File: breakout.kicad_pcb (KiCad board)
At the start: 2 copper layers, 103 x 62 mm, 32 parts, among them CON1 SD_Card, CON2 USB-MICRO-AB, P2 CONN_01X40, P3 CONN_01X40, P4 CONN_01X40, P5 A-DF-09-A/KG-T4S, Q1 SIA461DJ-T1-GE3, SW1 SW_PUSH

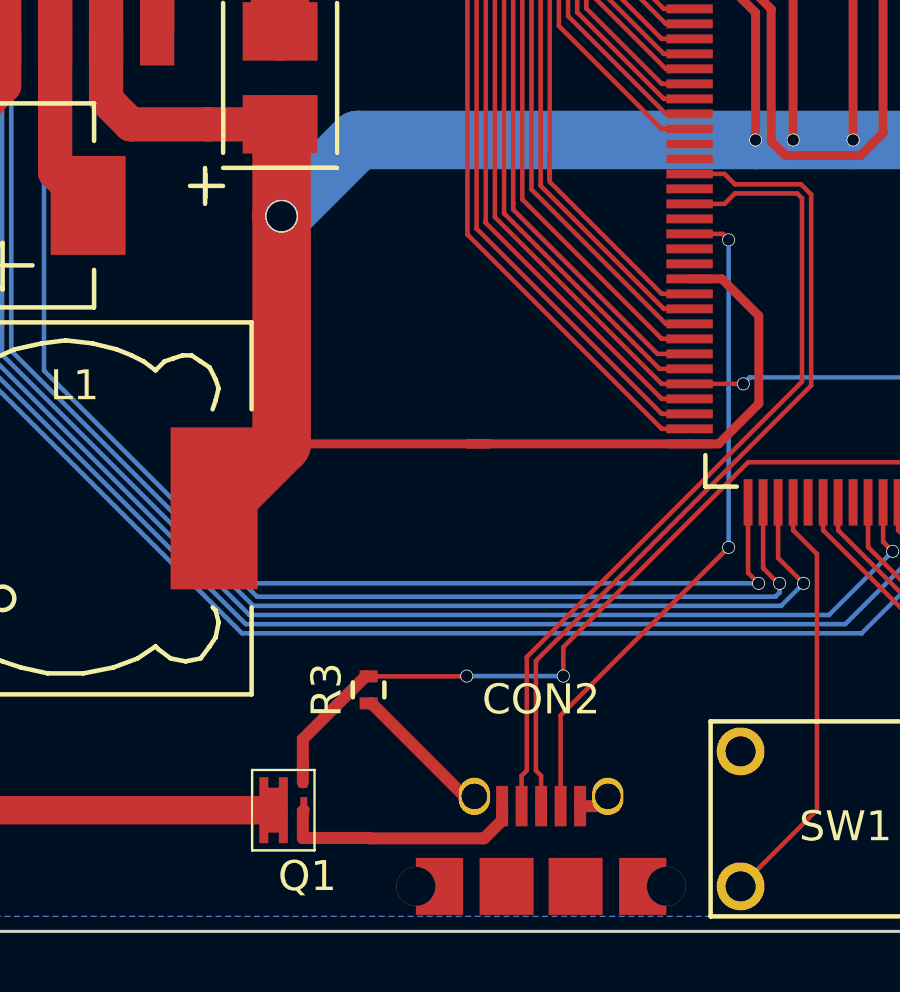
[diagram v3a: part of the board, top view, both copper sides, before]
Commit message: added USB FET to schematic and board
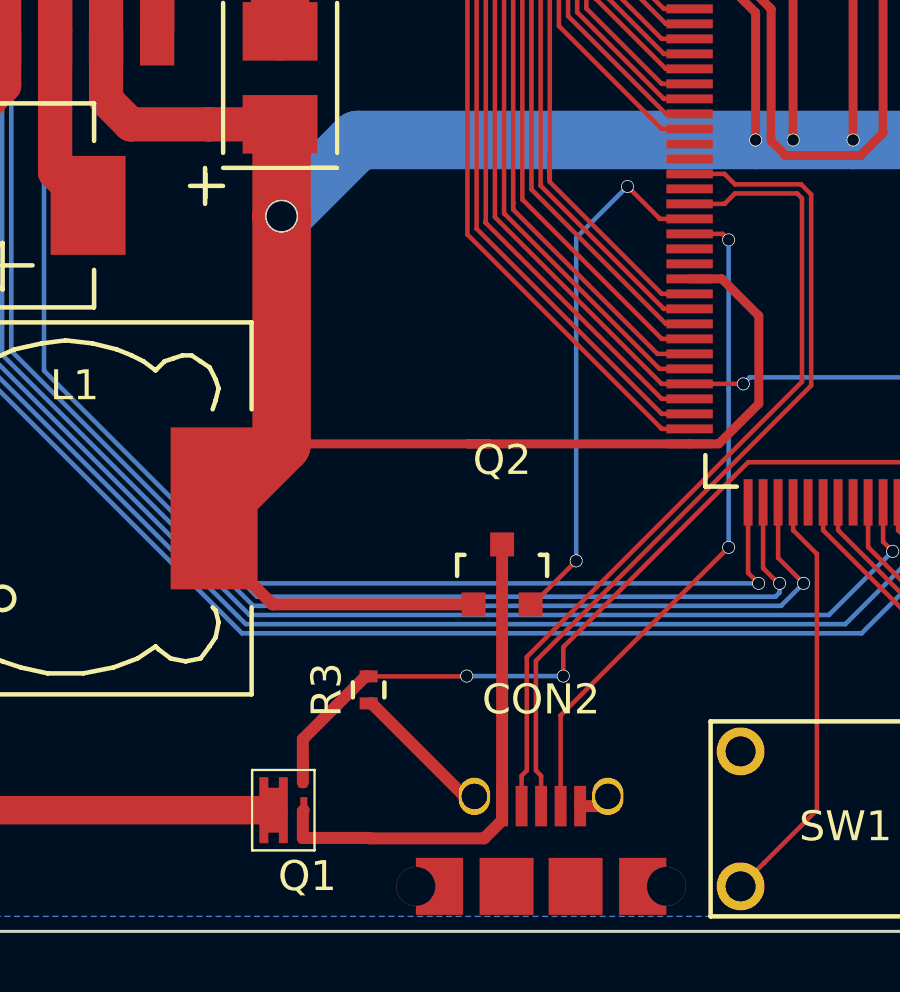
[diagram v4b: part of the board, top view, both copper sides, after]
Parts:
- added Q2: IRLML2402TRPBF, Housings_SOT-23_SOT-143_TSOT-6:SOT-23, F.Cu at (93.0, 163.1)
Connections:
- net Net-(CON2-Pad1) renamed /USB0_VBUS_PR
- CPU1 pad 21: (no net) -> /USB0_VBUS
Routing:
- net /USB0_VBUS: track 0.00 -> 17.8 mm, vias 0 -> 2
- net /3.3V: track 243.1 -> 253.8 mm
- net /USB0_VBUS_PR: track 8.31 -> 17.0 mm

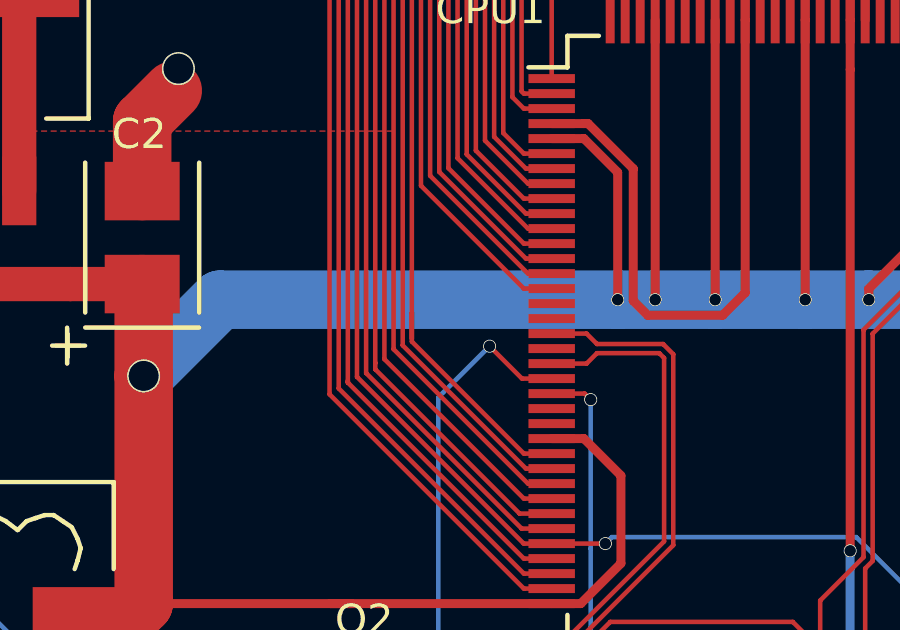
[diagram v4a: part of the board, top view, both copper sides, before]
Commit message: added USB0_RREF and 12K resistor
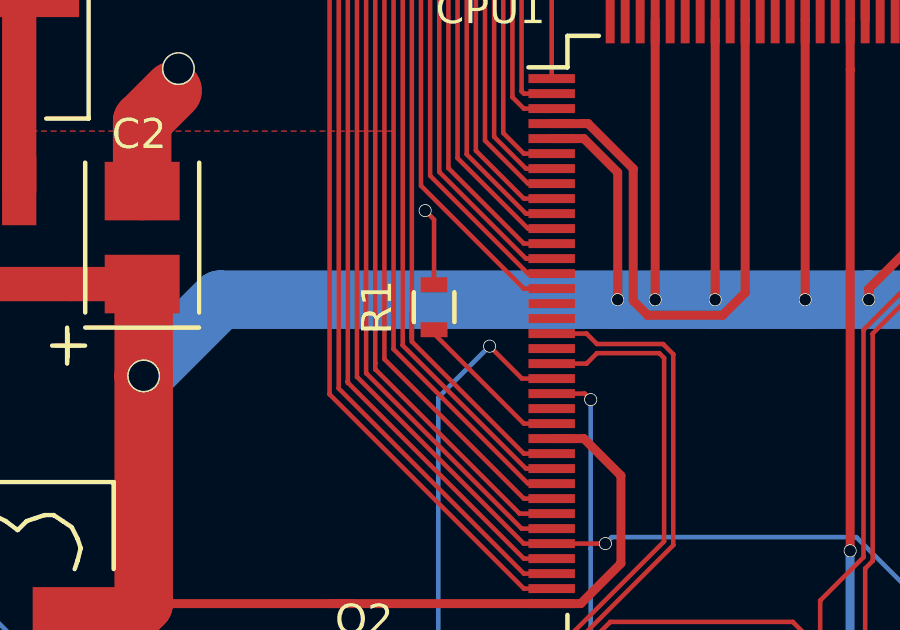
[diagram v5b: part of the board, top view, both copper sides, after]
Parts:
- added R1: 12K, Resistors_SMD:R_0603, F.Cu at (95.4, 148.9)
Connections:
- CPU1 pad 24: (no net) -> /USB0_RREF
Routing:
- net /USB0_RREF: track 0.00 -> 5.30 mm
- net GND: track 136.9 -> 139.5 mm, vias 8 -> 9

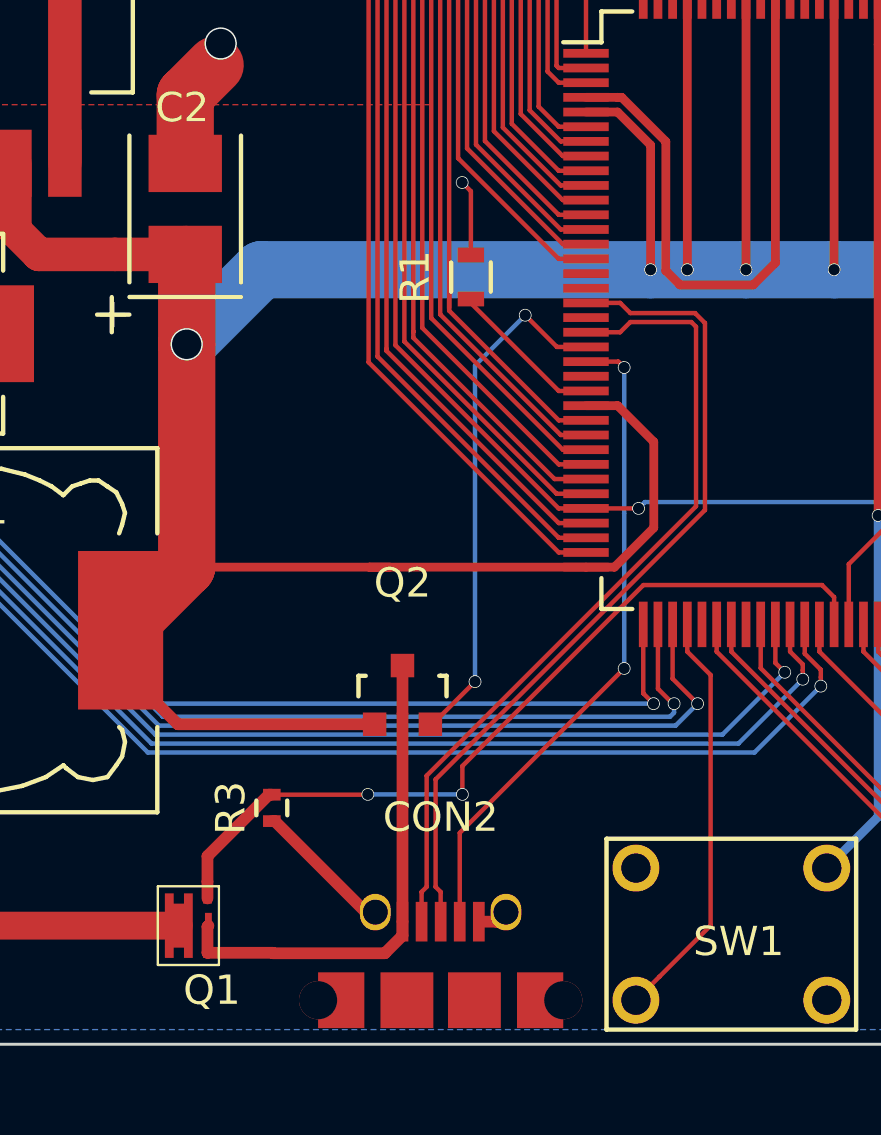
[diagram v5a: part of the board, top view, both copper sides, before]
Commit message: added the NC'd USB0 pins, and fixed some trace sizes
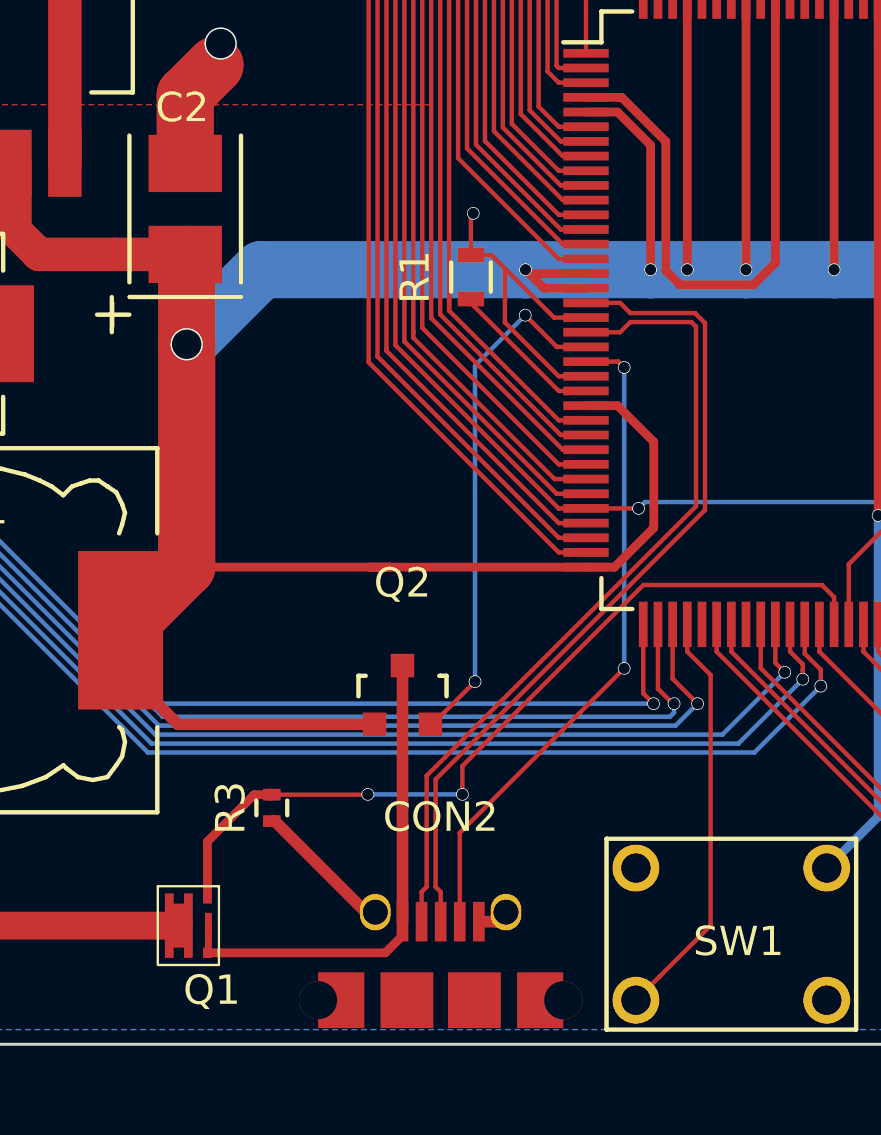
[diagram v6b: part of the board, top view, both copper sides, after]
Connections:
- CPU1 pad 16: (no net) -> /3.3V
- CPU1 pad 17: (no net) -> /3.3V
- CPU1 pad 19: (no net) -> GND
- CPU1 pad 23: (no net) -> GND
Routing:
- net GND: track 139.5 -> 148.6 mm
- net /3.3V: track 253.8 -> 258.3 mm, vias 10 -> 11
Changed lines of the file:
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@@
 (kicad_pcb (version 4) (host pcbnew "(after 2015-mar-04 BZR unknown)-product")
   (general
-    (links 234)
+    (links 238)
     (no_connects 19)
     (area 57.949999 112.949999 161.050001 175.050001)
     (thickness 1.6)
     (drawings 11)
-    (tracks 1106)
+    (tracks 1118)
     (zones 0)
     (modules 34)
@@
     (pad 15 smd rect (at -10.7 -1.75) (size 1.55 0.3) (layers F.Cu F.Paste F.Mask)
       (net 45 /P4_8))
-    (pad 16 smd rect (at -10.7 -1.25) (size 1.55 0.3) (layers F.Cu F.Paste F.Mask))
-    (pad 17 smd rect (at -10.7 -0.75) (size 1.55 0.3) (layers F.Cu F.Paste F.Mask))
+    (pad 16 smd rect (at -10.7 -1.25) (size 1.55 0.3) (layers F.Cu F.Paste F.Mask)
+      (net 4 /3.3V))
+    (pad 17 smd rect (at -10.7 -0.75) (size 1.55 0.3) (layers F.Cu F.Paste F.Mask)
+      (net 4 /3.3V))
     (pad 18 smd rect (at -10.7 -0.25) (size 1.55 0.3) (layers F.Cu F.Paste F.Mask)
       (net 29 /USB0_D+))
-    (pad 19 smd rect (at -10.7 0.25) (size 1.55 0.3) (layers F.Cu F.Paste F.Mask))
+    (pad 19 smd rect (at -10.7 0.25) (size 1.55 0.3) (layers F.Cu F.Paste F.Mask)
+      (net 1 GND))
     (pad 20 smd rect (at -10.7 0.75) (size 1.55 0.3) (layers F.Cu F.Paste F.Mask)
       (net 28 /USB0_D-))
@@
     (pad 22 smd rect (at -10.7 1.75) (size 1.55 0.3) (layers F.Cu F.Paste F.Mask)
       (net 30 /USB0_ID))
-    (pad 23 smd rect (at -10.7 2.25) (size 1.55 0.3) (layers F.Cu F.Paste F.Mask))
+    (pad 23 smd rect (at -10.7 2.25) (size 1.55 0.3) (layers F.Cu F.Paste F.Mask)
+      (net 1 GND))
     (pad 24 smd rect (at -10.7 2.75) (size 1.55 0.3) (layers F.Cu F.Paste F.Mask)
       (net 133 /USB0_RREF))
@@
   (gr_line (start 58 113) (end 161 113) (angle 90) (layer Edge.Cuts) (width 0.1))
   (segment (start 65.08 125.84114) (end 65.08 125) (width 0.1524) (layer F.Cu) (net 0))
-  (segment (start 95.38 148.12) (end 95.38 145.946811) (width 0.1524) (layer F.Cu) (net 1))
-  (segment (start 95.38 145.946811) (end 95.083189 145.65) (width 0.1524) (layer F.Cu) (net 1))
-  (via (at 95.083189 145.65) (size 0.4318) (drill 0.381) (layers F.Cu B.Cu) (net 1))
+  (segment (start 95.38 148.12) (end 95.38 146.78) (width 0.1524) (layer F.Cu) (net 1))
+  (segment (start 95.38 146.78) (end 95.46 146.7) (width 0.1524) (layer F.Cu) (net 1))
+  (via (at 95.46 146.7) (size 0.4318) (drill 0.381) (layers F.Cu B.Cu) (net 1))
+  (segment (start 98.212099 150.25) (end 96.537853 148.575754) (width 0.1524) (layer F.Cu) (net 1))
+  (segment (start 96.537853 148.575754) (end 96.082099 148.12) (width 0.1524) (layer F.Cu) (net 1))
+  (segment (start 99.3 152.25) (end 98.3726 152.25) (width 0.1524) (layer F.Cu) (net 1))
+  (segment (start 98.3726 152.25) (end 96.537853 150.415253) (width 0.1524) (layer F.Cu) (net 1))
+  (segment (start 96.537853 150.415253) (end 96.537853 148.575754) (width 0.1524) (layer F.Cu) (net 1))
+  (segment (start 99.3 150.25) (end 98.212099 150.25) (width 0.1524) (layer F.Cu) (net 1))
+  (segment (start 96.082099 148.12) (end 95.9824 148.12) (width 0.1524) (layer F.Cu) (net 1))
+  (segment (start 95.9824 148.12) (end 95.38 148.12) (width 0.1524) (layer F.Cu) (net 1))
   (segment (start 88.6 167.4) (end 88.7 167.4) (width 0.4) (layer F.Cu) (net 1))
   (segment (start 88.7 167.4) (end 91.8 170.5) (width 0.4) (layer F.Cu) (net 1))
@@
   (segment (start 102.75 139.3) (end 102.75 148.62) (width 0.3) (layer F.Cu) (net 4))
   (via (at 102.75 148.62) (size 0.4318) (drill 0.381) (layers F.Cu B.Cu) (net 4))
-  (segment (start 88.24 148.62) (end 101.500445 148.62) (width 1.95072) (layer B.Cu) (net 4))
   (segment (start 100.375 143.25) (end 101.500445 144.375445) (width 0.3) (layer F.Cu) (net 4))
   (segment (start 99.3 143.25) (end 100.375 143.25) (width 0.3) (layer F.Cu) (net 4))
@@
   (segment (start 85.40108 164.10076) (end 83.45 162.14968) (width 0.4) (layer F.Cu) (net 4))
   (segment (start 92.1 164.10076) (end 85.40108 164.10076) (width 0.4) (layer F.Cu) (net 4))
+  (via (at 97.239961 148.62) (size 0.4318) (drill 0.381) (layers F.Cu B.Cu) (net 4))
+  (segment (start 97.869961 149.25) (end 97.239961 148.62) (width 0.3) (layer F.Cu) (net 4))
+  (segment (start 99.3 149.25) (end 97.869961 149.25) (width 0.3) (layer F.Cu) (net 4))
+  (segment (start 97.239961 148.62) (end 101.500445 148.62) (width 1.95072) (layer B.Cu) (net 4))
+  (segment (start 88.24 148.62) (end 97.239961 148.62) (width 1.95072) (layer B.Cu) (net 4))
+  (segment (start 97.369961 148.75) (end 97.239961 148.62) (width 0.3) (layer F.Cu) (net 4))
+  (segment (start 99.3 148.75) (end 97.369961 148.75) (width 0.3) (layer F.Cu) (net 4))
   (segment (start 122.2 157.7) (end 120.75 157.7) (width 0.1524) (layer F.Cu) (net 5))
   (segment (start 120.75 157.7) (end 120.7 157.75) (width 0.1524) (layer F.Cu) (net 5))
@@
   (segment (start 60.8787 168.68188) (end 60.1287 169.43188) (width 0.3) (layer F.Cu) (net 16))
   (segment (start 60.1287 169.43188) (end 60.1287 170.179964) (width 0.3) (layer F.Cu) (net 16))
+  (segment (start 86.4075 170.035) (end 86.4075 168.0925) (width 0.3) (layer F.Cu) (net 17))
+  (segment (start 86.4075 168.0925) (end 88 166.5) (width 0.3) (layer F.Cu) (net 17))
+  (segment (start 88 166.5) (end 88.6 166.5) (width 0.3) (layer F.Cu) (net 17))
   (segment (start 88.6 166.5) (end 88.5 166.5) (width 0.4) (layer F.Cu) (net 17))
-  (segment (start 88.5 166.5) (end 86.4075 168.5925) (width 0.4) (layer F.Cu) (net 17))
-  (segment (start 86.4075 168.5925) (end 86.4075 169.46) (width 0.4) (layer F.Cu) (net 17))
-  (segment (start 86.4075 169.46) (end 86.4075 170.035) (width 0.4) (layer F.Cu) (net 17))
   (segment (start 95.09 166.49) (end 95.09 165.523518) (width 0.1524) (layer F.Cu) (net 17))
   (segment (start 95.09 165.523518) (end 101.253518 159.36) (width 0.1524) (layer F.Cu) (net 17))
@@
   (segment (start 72.7 121.1684) (end 72.7 120) (width 0.1524) (layer B.Cu) (net 130))
   (segment (start 73.84298 122.31138) (end 72.7 121.1684) (width 0.1524) (layer B.Cu) (net 130))
-  (segment (start 86.4075 171.885) (end 86.4075 170.9925) (width 0.4) (layer F.Cu) (net 131))
-  (segment (start 86.4075 170.9925) (end 86.44 170.96) (width 0.4) (layer F.Cu) (net 131))
-  (segment (start 88.64 171.9) (end 88.625 171.885) (width 0.4) (layer F.Cu) (net 131))
-  (segment (start 88.625 171.885) (end 86.4075 171.885) (width 0.4) (layer F.Cu) (net 131))
-  (segment (start 92.45 171.9) (end 93.05 171.3) (width 0.4) (layer F.Cu) (net 131))
-  (segment (start 88.64 171.9) (end 92.45 171.9) (width 0.4) (layer F.Cu) (net 131))
-  (segment (start 93.05 171.3) (end 93.05 170.825) (width 0.4) (layer F.Cu) (net 131))
+  (segment (start 86.4075 171.885) (end 92.465 171.885) (width 0.3) (layer F.Cu) (net 131))
+  (segment (start 92.465 171.885) (end 93.05 171.3) (width 0.3) (layer F.Cu) (net 131))
+  (segment (start 93.05 171.3) (end 93.05 170.825) (width 0.3) (layer F.Cu) (net 131))
+  (segment (start 86.44 170.96) (end 86.44 171.8525) (width 0.235) (layer F.Cu) (net 131))
+  (segment (start 86.44 171.8525) (end 86.4075 171.885) (width 0.235) (layer F.Cu) (net 131))
   (segment (start 93.05 163.753498) (end 93.05 162.10178) (width 0.4) (layer F.Cu) (net 131))
   (segment (start 93.05 170.825) (end 93.05 163.753498) (width 0.4) (layer F.Cu) (net 131))

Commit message: added test points
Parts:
- added W2: TEST, Measurement_Points:Measurement_Point_Round-SMD-Pad_Small, F.Cu at (96.3, 166.0)
- added W3: TEST, Measurement_Points:Measurement_Point_Round-SMD-Pad_Small, F.Cu at (96.0, 161.0)
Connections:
- R4 pad 2: /3.3V -> (no net)
- R6 pad 2: /3.3V -> (no net)
- R7 pad 2: /3.3V -> (no net)
- R8 pad 2: /3.3V -> (no net)
- R9 pad 2: /3.3V -> (no net)
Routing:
- net /USB0_VBUS: track 17.8 -> 19.6 mm
- net /USB0_PPWR: track 28.7 -> 30.2 mm
